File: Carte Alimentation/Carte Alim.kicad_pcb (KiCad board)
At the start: 2 copper layers, 102.9 x 70.5 mm, 58 parts, among them K1 CONN_3, P1 CONN_2, P10 CONN_2, P11 CONN_2, P12 CONN_2, P13 CONN_4, P2 CONN_2, P3 CONN_2, P4 CONN_5, P5 CONN_1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

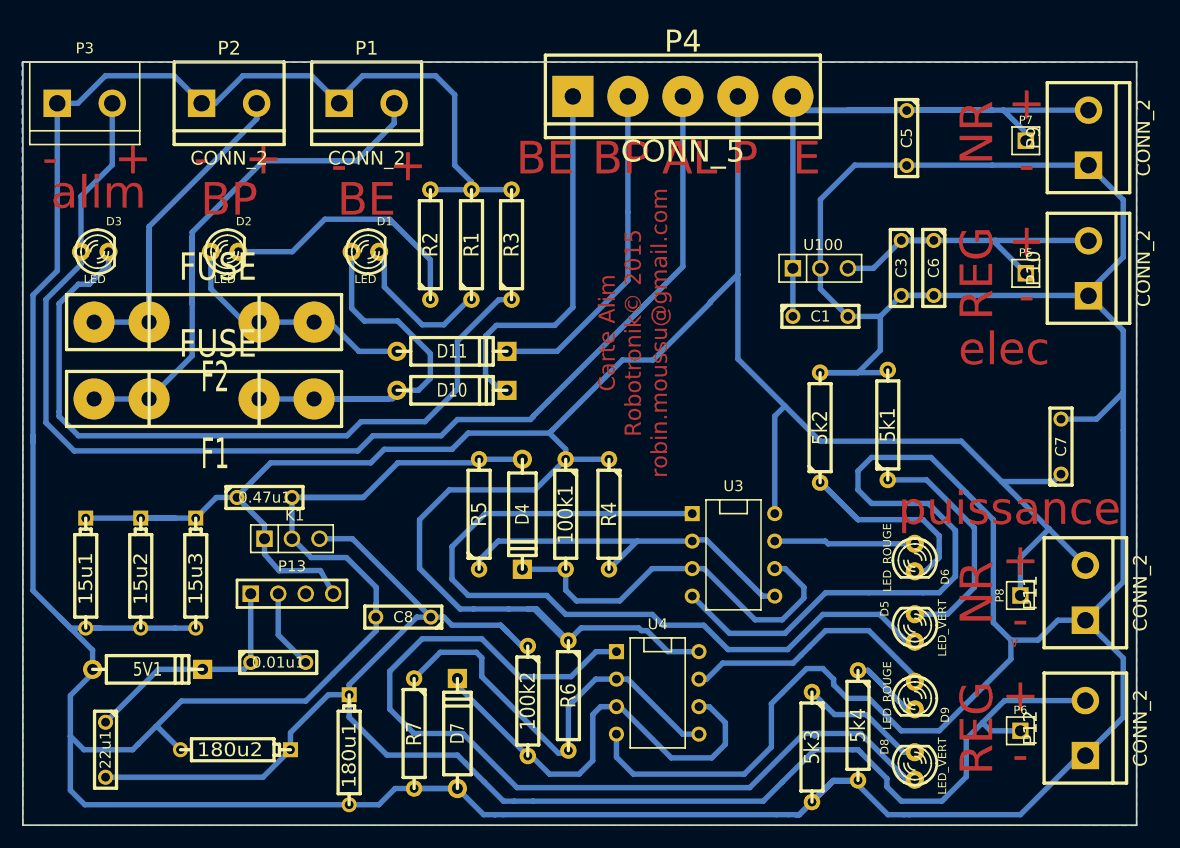
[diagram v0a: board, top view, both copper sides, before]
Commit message: correction norme bornier alim
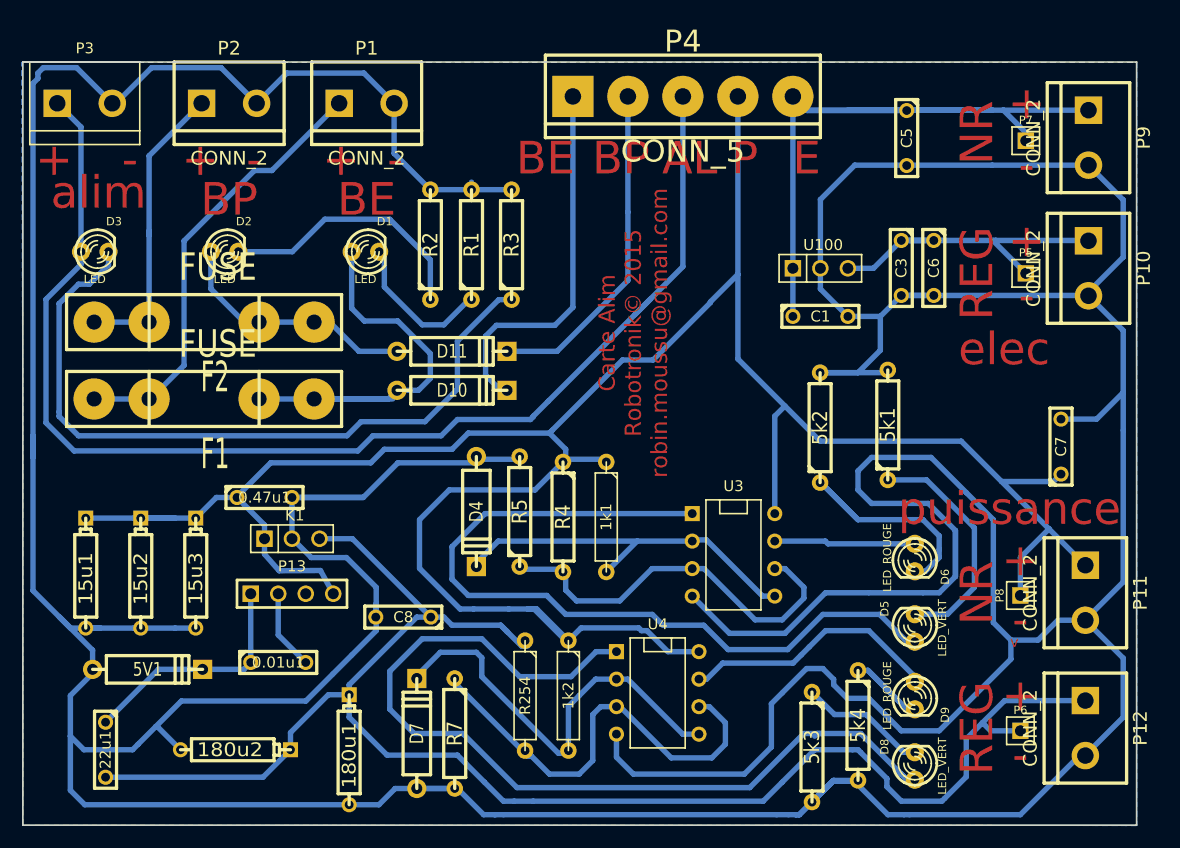
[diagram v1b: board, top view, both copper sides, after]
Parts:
- removed 100k1, 100k2, R6: R, R4
- added 1k1: R, Discret:R4, F.Cu at (116.8, 199.5)
- added 1k2: R, Discret:R4, F.Cu at (113.2, 216.0)
- added R254: R, Discret:R4, F.Cu at (109.2, 216.0)
- moved D4 4.26 mm to (104.8, 199.0)
- moved R4 4.26 mm to (112.8, 199.5)
- moved R5 3.76 mm to (108.8, 199.0)
- moved D7 3.75 mm to (99.2, 219.5)
- moved R7 3.75 mm to (102.8, 219.5)
- turned P10 to 270 degrees
- turned P11 to 270 degrees
- turned P12 to 270 degrees
- turned P9 to 270 degrees
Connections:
- D4 pad 2: Net-(100k1-Pad2) -> Net-(1k1-Pad2)
- D7 pad 2: Net-(100k2-Pad2) -> Net-(1k2-Pad2)
- P1 pad 1: GND -> Net-(F1-Pad1)
- P1 pad 2: Net-(F1-Pad1) -> GND
- P10 pad 1: GND -> /alim_elec
- P10 pad 2: /alim_elec -> GND
- P11 pad 1: GND -> /alim_puissance_non_regul
- P11 pad 2: /alim_puissance_non_regul -> GND
- P12 pad 1: GND -> /alim_puissance_regul
- P12 pad 2: /alim_puissance_regul -> GND
- P2 pad 1: GND -> Net-(F2-Pad1)
- P2 pad 2: Net-(F2-Pad1) -> GND
- P3 pad 1: GND -> Net-(D3-Pad1)
- P3 pad 2: Net-(D3-Pad1) -> GND
- P9 pad 1: GND -> /alim_elec_non_regul
- P9 pad 2: /alim_elec_non_regul -> GND
- R7 pad 1: Net-(R6-Pad2) -> Net-(R254-Pad2)
- U3 pad 2: Net-(R4-Pad2) -> Net-(1k1-Pad2)
- U3 pad 3: Net-(100k1-Pad2) -> Net-(R4-Pad2)
- U3 pad 5: Net-(R4-Pad2) -> Net-(1k1-Pad2)
- U3 pad 6: Net-(100k1-Pad2) -> Net-(R4-Pad2)
- U4 pad 2: Net-(R6-Pad2) -> Net-(1k2-Pad2)
- U4 pad 3: Net-(100k2-Pad2) -> Net-(R254-Pad2)
- U4 pad 5: Net-(R6-Pad2) -> Net-(1k2-Pad2)
- U4 pad 6: Net-(100k2-Pad2) -> Net-(R254-Pad2)
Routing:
- net Net-(R254-Pad2): track 0.00 -> 41.5 mm
- net Net-(100k2-Pad2): track 41.5 -> 0.00 mm
- net Net-(R6-Pad2): track 40.0 -> 0.00 mm
- net Net-(1k2-Pad2): track 0.00 -> 40.0 mm
- net Net-(100k1-Pad2): track 37.5 -> 0.00 mm
- net Net-(1k1-Pad2): track 0.00 -> 34.7 mm
- net Net-(F1-Pad1): track 53.0 -> 41.1 mm
- net Net-(F2-Pad1): track 39.3 -> 27.7 mm
- net Net-(R4-Pad2): track 34.7 -> 37.5 mm
- net GND: track 626.3 -> 628.2 mm

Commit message: some clean carte alim + export
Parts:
- removed U100: 7905_CORRIGE, PIN_ARRAY_3X1
- moved C1 104.0 mm to (172.8, 83.5), turned to 270 degrees
- moved D2 92.4 mm to (113.8, 88.5)
- moved D1 92.3 mm to (126.6, 88.5)
- moved D3 91.8 mm to (100.3, 88.5)
- moved 0.47u1 91.8 mm to (129.8, 117.5), turned to 270 degrees
- moved F2 91.1 mm to (112.3, 96.5)
- moved 15u1 90.8 mm to (101.3, 120.0)
- moved 15u2 90.6 mm to (105.8, 120.0)
- moved 15u3 90.5 mm to (110.8, 120.0)
- moved D10 90.4 mm to (135.1, 103.5)
- moved R2 90.0 mm to (140.1, 93.5)
- moved 5V1 89.0 mm to (104.8, 130.0)
- moved F1 88.9 mm to (112.3, 106.0)
- moved R3 88.4 mm to (143.8, 93.5)
- moved P11 88.0 mm to (194.2, 125.0)
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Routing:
- net /alim_elec_non_regul: track 76.2 -> 35.9 mm
- net GND: track 628.2 -> 618.7 mm
- net Net-(D2-Pad2): track 24.2 -> 33.0 mm
- net Net-(D10-Pad2): track 34.8 -> 26.5 mm
- net Net-(D3-Pad2): track 68.1 -> 75.6 mm
- net Net-(D11-Pad1): track 23.0 -> 28.7 mm
- net Net-(0.01u1-Pad1): track 22.0 -> 27.5 mm
- net /alim_elec: track 34.9 -> 30.0 mm
- net Net-(F2-Pad1): track 27.7 -> 23.2 mm
- net Net-(D3-Pad1): track 116.4 -> 112.6 mm
- net Net-(F1-Pad1): track 41.1 -> 44.5 mm
- net /alim_puissance_regul: track 149.4 -> 146.1 mm
- net /alim_puissance_non_regul: track 237.9 -> 240.7 mm
- net Net-(D11-Pad2): track 30.9 -> 32.2 mm
- net Net-(1k2-Pad2): track 40.0 -> 38.9 mm
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- added copper zone on F.Cu, net GND
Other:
- board text added: "Carte Alimentation Robotronik 2014-2015"
- board text added: "Puissance"
- board text added: "Rég"
- board text added: "Élec"
- board text removed: "Carte Alim Robotronik© 2015 robin.moussu@gmail.com"
- board text removed: "REG"
- board text removed: "elec"
- board text removed: "puissance"
- board text removed: "v"
